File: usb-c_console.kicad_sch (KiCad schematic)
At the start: 28 parts, among them J3 USB-C_Kycon_KUSBX-SL2-CS1N24-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, U6 FT230X_QFN, U7 NTS0102_TSSOP

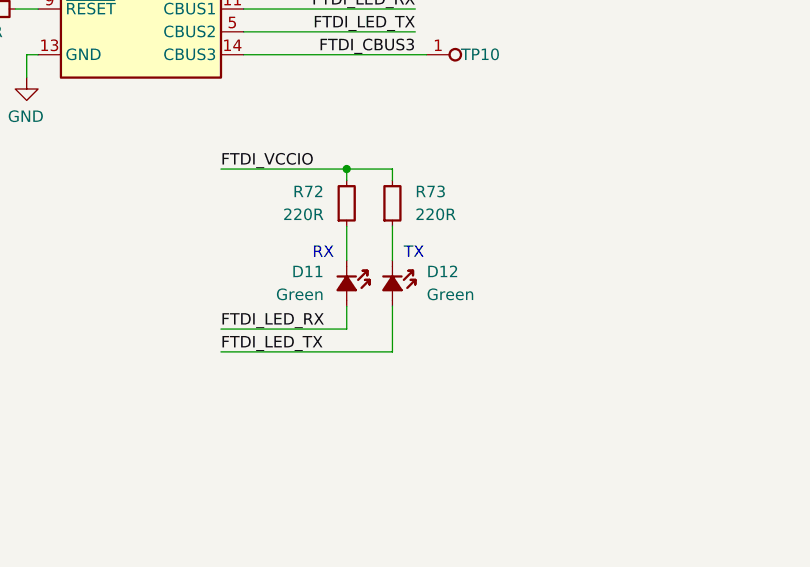
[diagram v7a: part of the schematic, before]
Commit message: [#65447] Fix rotated LEDs, overlapping text and symbols, add rules
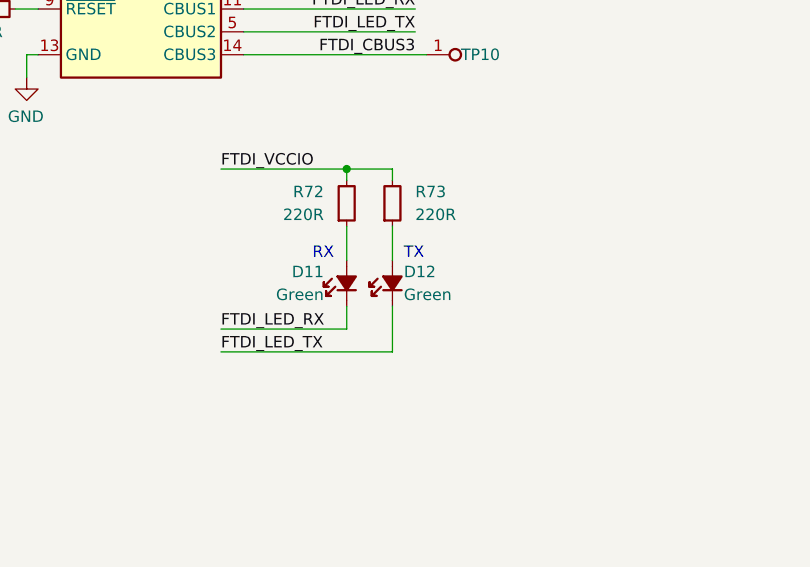
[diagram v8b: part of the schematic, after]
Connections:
- net FTDI_LED_RX: now also D11.1 (C); no longer D11.2 (A)
- net FTDI_LED_TX: now also D12.1 (C); no longer D12.2 (A)
- net at R72.1: now also D11.2 (A); no longer D11.1 (C)
- net at R73.1: now also D12.2 (A); no longer D12.1 (C)
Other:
- moved on the sheet: D11, D12
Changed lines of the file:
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@@
     )
   )
-  (symbol (lib_id "antmicroLEDIndicationDiscrete:LED_G_0603_LTST-C190GKT") (at 229.87 171.45 270) (unit 1)
-    (in_bom yes) (on_board yes) (dnp no) (fields_autoplaced)
-    (property "Reference" "D12" (at 233.68 172.72 90)
-      (effects (font (size 1.27 1.27)) (justify left))
-    )
-    (property "Value" "LED_G_0603_LTST-C190GKT" (at 222.25 194.31 0)
-      (effects (font (size 1.27 1.27) (thickness 0.15)) (justify left bottom) hide)
-    )
-    (property "Footprint" "antmicro-footprints:LED_0603_1608Metric_G" (at 219.71 194.31 0)
-      (effects (font (size 1.27 1.27) (thickness 0.15)) (justify left bottom) hide)
-    )
-    (property "Datasheet" "https://media.digikey.com/pdf/Data%20Sheets/Lite-On%20PDFs/LTST-C190GKT.pdf" (at 217.17 194.31 0)
-      (effects (font (size 1.27 1.27) (thickness 0.15)) (justify left bottom) hide)
-    )
-    (property "MPN" "LTST-C190GKT" (at 233.68 176.5299 90)
+  (symbol (lib_id "antmicroLEDIndicationDiscrete:LED_G_0603_LTST-C190GKT") (at 229.87 176.53 90) (unit 1)
+    (in_bom yes) (on_board yes) (dnp no)
+    (property "Reference" "D12" (at 231.14 172.72 90)
+      (effects (font (size 1.27 1.27)) (justify right))
+    )
+    (property "Value" "LED_G_0603_LTST-C190GKT" (at 237.49 153.67 0)
+      (effects (font (size 1.27 1.27) (thickness 0.15)) (justify left bottom) hide)
+    )
+    (property "Footprint" "antmicro-footprints:LED_0603_1608Metric_G" (at 240.03 153.67 0)
+      (effects (font (size 1.27 1.27) (thickness 0.15)) (justify left bottom) hide)
+    )
+    (property "Datasheet" "https://media.digikey.com/pdf/Data%20Sheets/Lite-On%20PDFs/LTST-C190GKT.pdf" (at 242.57 153.67 0)
+      (effects (font (size 1.27 1.27) (thickness 0.15)) (justify left bottom) hide)
+    )
+    (property "MPN" "LTST-C190GKT" (at 226.06 171.4501 90)
       (effects (font (size 1.27 1.27) (thickness 0.15)) (justify left) hide)
     )
-    (property "Manufacturer" "Lite-On" (at 212.09 194.31 0)
-      (effects (font (size 1.27 1.27) (thickness 0.15)) (justify left bottom) hide)
-    )
-    (property "Author" "Antmicro" (at 209.55 194.31 0)
-      (effects (font (size 1.27 1.27) (thickness 0.15)) (justify left bottom) hide)
-    )
-    (property "License" "Apache-2.0" (at 207.01 194.31 0)
-      (effects (font (size 1.27 1.27) (thickness 0.15)) (justify left bottom) hide)
-    )
-    (property "Public" "False" (at 212.09 191.77 0)
-      (effects (font (size 1.27 1.27)) (justify left bottom) hide)
-    )
-    (property "Color" "Green" (at 233.68 175.26 90)
-      (effects (font (size 1.27 1.27)) (justify left))
+    (property "Manufacturer" "Lite-On" (at 247.65 153.67 0)
+      (effects (font (size 1.27 1.27) (thickness 0.15)) (justify left bottom) hide)
+    )
+    (property "Author" "Antmicro" (at 250.19 153.67 0)
+      (effects (font (size 1.27 1.27) (thickness 0.15)) (justify left bottom) hide)
+    )
+    (property "License" "Apache-2.0" (at 252.73 153.67 0)
+      (effects (font (size 1.27 1.27) (thickness 0.15)) (justify left bottom) hide)
+    )
+    (property "Public" "False" (at 247.65 156.21 0)
+      (effects (font (size 1.27 1.27)) (justify left bottom) hide)
+    )
+    (property "Color" "Green" (at 231.14 175.26 90)
+      (effects (font (size 1.27 1.27)) (justify right))
     )
     (pin "1")
@@
     )
   )
-  (symbol (lib_id "antmicroLEDIndicationDiscrete:LED_G_0603_LTST-C190GKT") (at 224.79 171.45 270) (unit 1)
+  (symbol (lib_id "antmicroLEDIndicationDiscrete:LED_G_0603_LTST-C190GKT") (at 224.79 176.53 90) (unit 1)
     (in_bom yes) (on_board yes) (dnp no)
     (property "Reference" "D11" (at 222.25 172.72 90)
-      (effects (font (size 1.27 1.27)) (justify right))
-    )
-    (property "Value" "LED_G_0603_LTST-C190GKT" (at 217.17 194.31 0)
-      (effects (font (size 1.27 1.27) (thickness 0.15)) (justify left bottom) hide)
-    )
-    (property "Footprint" "antmicro-footprints:LED_0603_1608Metric_G" (at 214.63 194.31 0)
-      (effects (font (size 1.27 1.27) (thickness 0.15)) (justify left bottom) hide)
-    )
-    (property "Datasheet" "https://media.digikey.com/pdf/Data%20Sheets/Lite-On%20PDFs/LTST-C190GKT.pdf" (at 212.09 194.31 0)
-      (effects (font (size 1.27 1.27) (thickness 0.15)) (justify left bottom) hide)
-    )
-    (property "MPN" "LTST-C190GKT" (at 228.6 176.5299 90)
+      (effects (font (size 1.27 1.27)) (justify left))
+    )
+    (property "Value" "LED_G_0603_LTST-C190GKT" (at 232.41 153.67 0)
+      (effects (font (size 1.27 1.27) (thickness 0.15)) (justify left bottom) hide)
+    )
+    (property "Footprint" "antmicro-footprints:LED_0603_1608Metric_G" (at 234.95 153.67 0)
+      (effects (font (size 1.27 1.27) (thickness 0.15)) (justify left bottom) hide)
+    )
+    (property "Datasheet" "https://media.digikey.com/pdf/Data%20Sheets/Lite-On%20PDFs/LTST-C190GKT.pdf" (at 237.49 153.67 0)
+      (effects (font (size 1.27 1.27) (thickness 0.15)) (justify left bottom) hide)
+    )
+    (property "MPN" "LTST-C190GKT" (at 220.98 171.4501 90)
       (effects (font (size 1.27 1.27) (thickness 0.15)) (justify left) hide)
     )
-    (property "Manufacturer" "Lite-On" (at 207.01 194.31 0)
-      (effects (font (size 1.27 1.27) (thickness 0.15)) (justify left bottom) hide)
-    )
-    (property "Author" "Antmicro" (at 204.47 194.31 0)
-      (effects (font (size 1.27 1.27) (thickness 0.15)) (justify left bottom) hide)
-    )
-    (property "License" "Apache-2.0" (at 201.93 194.31 0)
-      (effects (font (size 1.27 1.27) (thickness 0.15)) (justify left bottom) hide)
-    )
-    (property "Public" "False" (at 207.01 191.77 0)
+    (property "Manufacturer" "Lite-On" (at 242.57 153.67 0)
+      (effects (font (size 1.27 1.27) (thickness 0.15)) (justify left bottom) hide)
+    )
+    (property "Author" "Antmicro" (at 245.11 153.67 0)
+      (effects (font (size 1.27 1.27) (thickness 0.15)) (justify left bottom) hide)
+    )
+    (property "License" "Apache-2.0" (at 247.65 153.67 0)
+      (effects (font (size 1.27 1.27) (thickness 0.15)) (justify left bottom) hide)
+    )
+    (property "Public" "False" (at 242.57 156.21 0)
       (effects (font (size 1.27 1.27)) (justify left bottom) hide)
     )
     (property "Color" "Green" (at 222.25 175.26 90)
-      (effects (font (size 1.27 1.27)) (justify right))
-    )
-    (pin "1")
+      (effects (font (size 1.27 1.27)) (justify left))
+    )
+    (pin "1")
